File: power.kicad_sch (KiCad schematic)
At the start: 25 parts

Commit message: Assign 0603 footprints to all resistors
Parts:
- C66: footprint (none) -> Capacitor_SMD:C_0603_1608Metric_Pad1.08x0.95mm_HandSolder
- R10, R11, R8, R9: footprint (none) -> Resistor_SMD:R_0603_1608Metric_Pad0.98x0.95mm_HandSolder
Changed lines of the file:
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@@
 			)
 		)
-		(property "Footprint" ""
+		(property "Footprint" "Resistor_SMD:R_0603_1608Metric_Pad0.98x0.95mm_HandSolder"
 			(at 83.058 81.28 90)
 			(effects
@@
 			)
 		)
-		(property "Footprint" ""
+		(property "Footprint" "Resistor_SMD:R_0603_1608Metric_Pad0.98x0.95mm_HandSolder"
 			(at 111.252 69.85 90)
 			(effects
@@
 			)
 		)
-		(property "Footprint" ""
+		(property "Footprint" "Resistor_SMD:R_0603_1608Metric_Pad0.98x0.95mm_HandSolder"
 			(at 83.058 66.04 90)
 			(effects
@@
 			)
 		)
-		(property "Footprint" ""
+		(property "Footprint" "Capacitor_SMD:C_0603_1608Metric_Pad1.08x0.95mm_HandSolder"
 			(at 133.0452 132.08 0)
 			(effects
@@
 			)
 		)
-		(property "Footprint" ""
+		(property "Footprint" "Resistor_SMD:R_0603_1608Metric_Pad0.98x0.95mm_HandSolder"
 			(at 203.962 132.08 90)
 			(effects

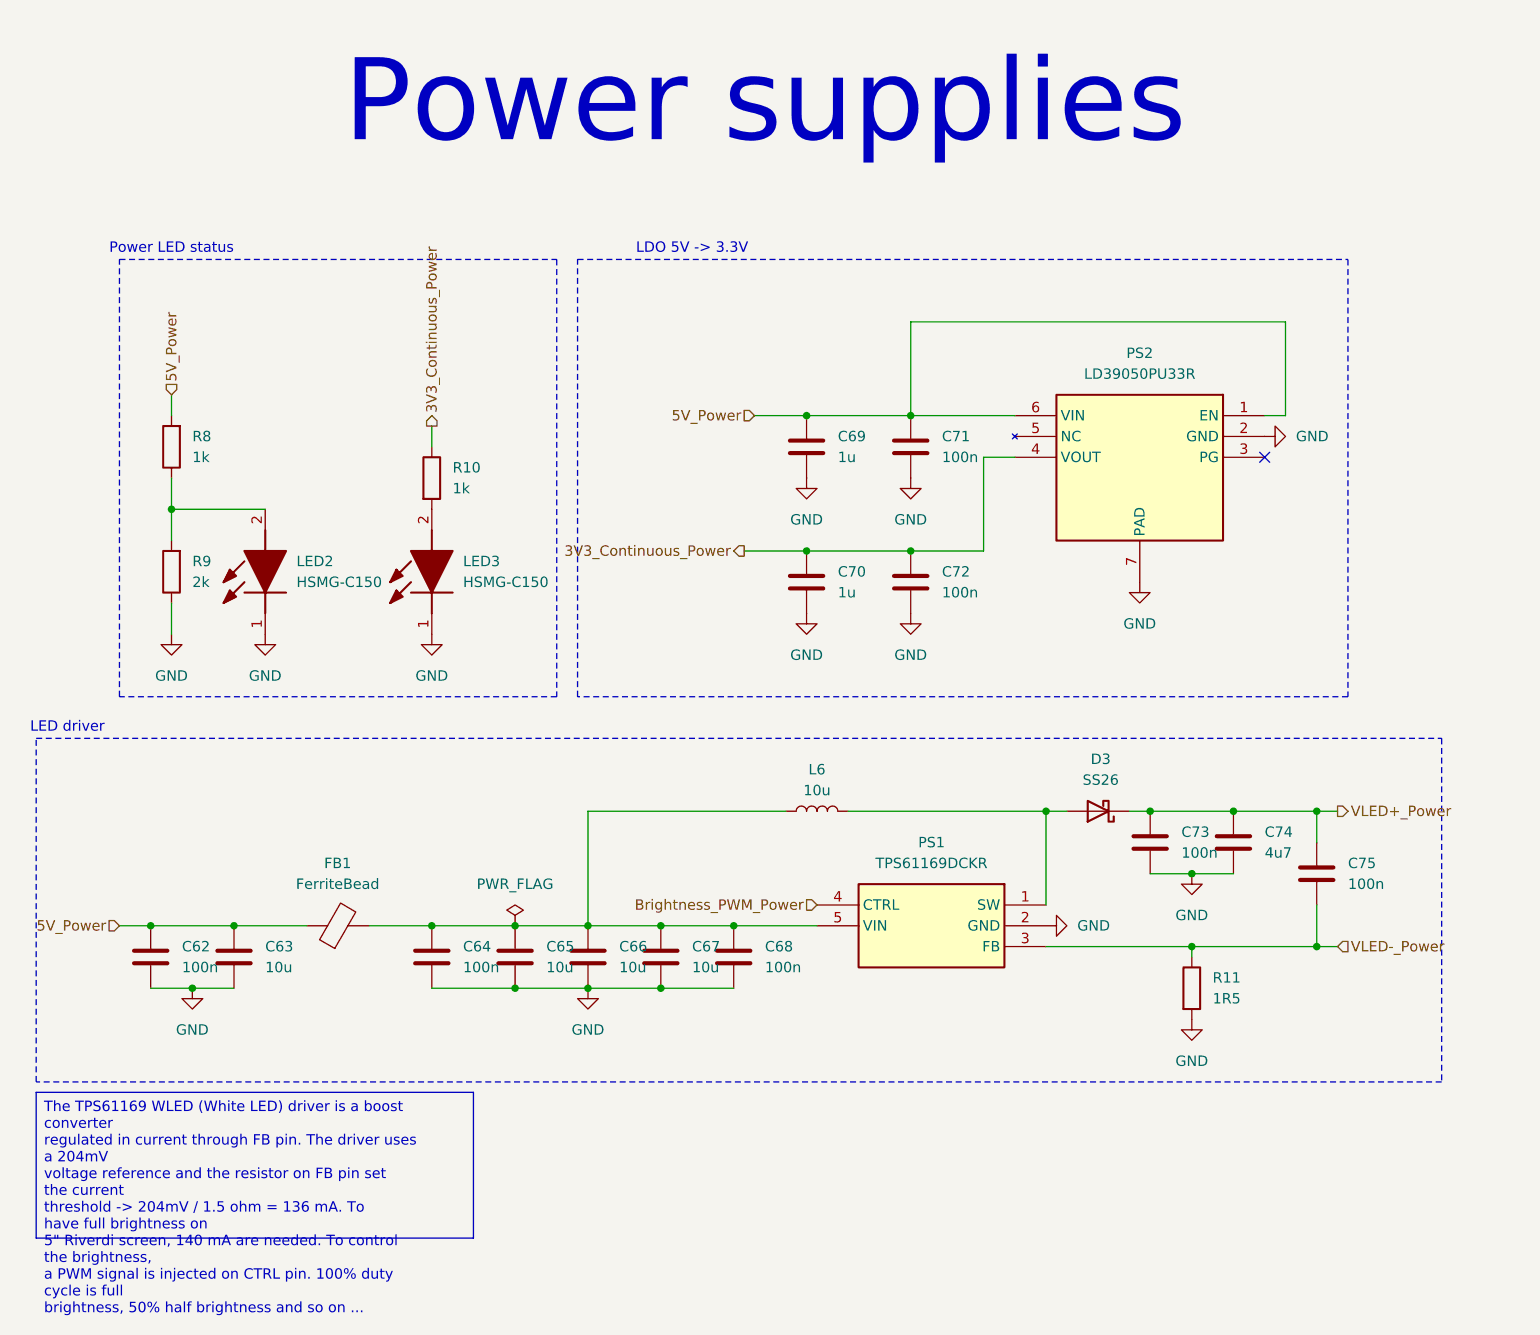
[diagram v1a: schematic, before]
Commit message: Add SS26FL diode for LCD power supply
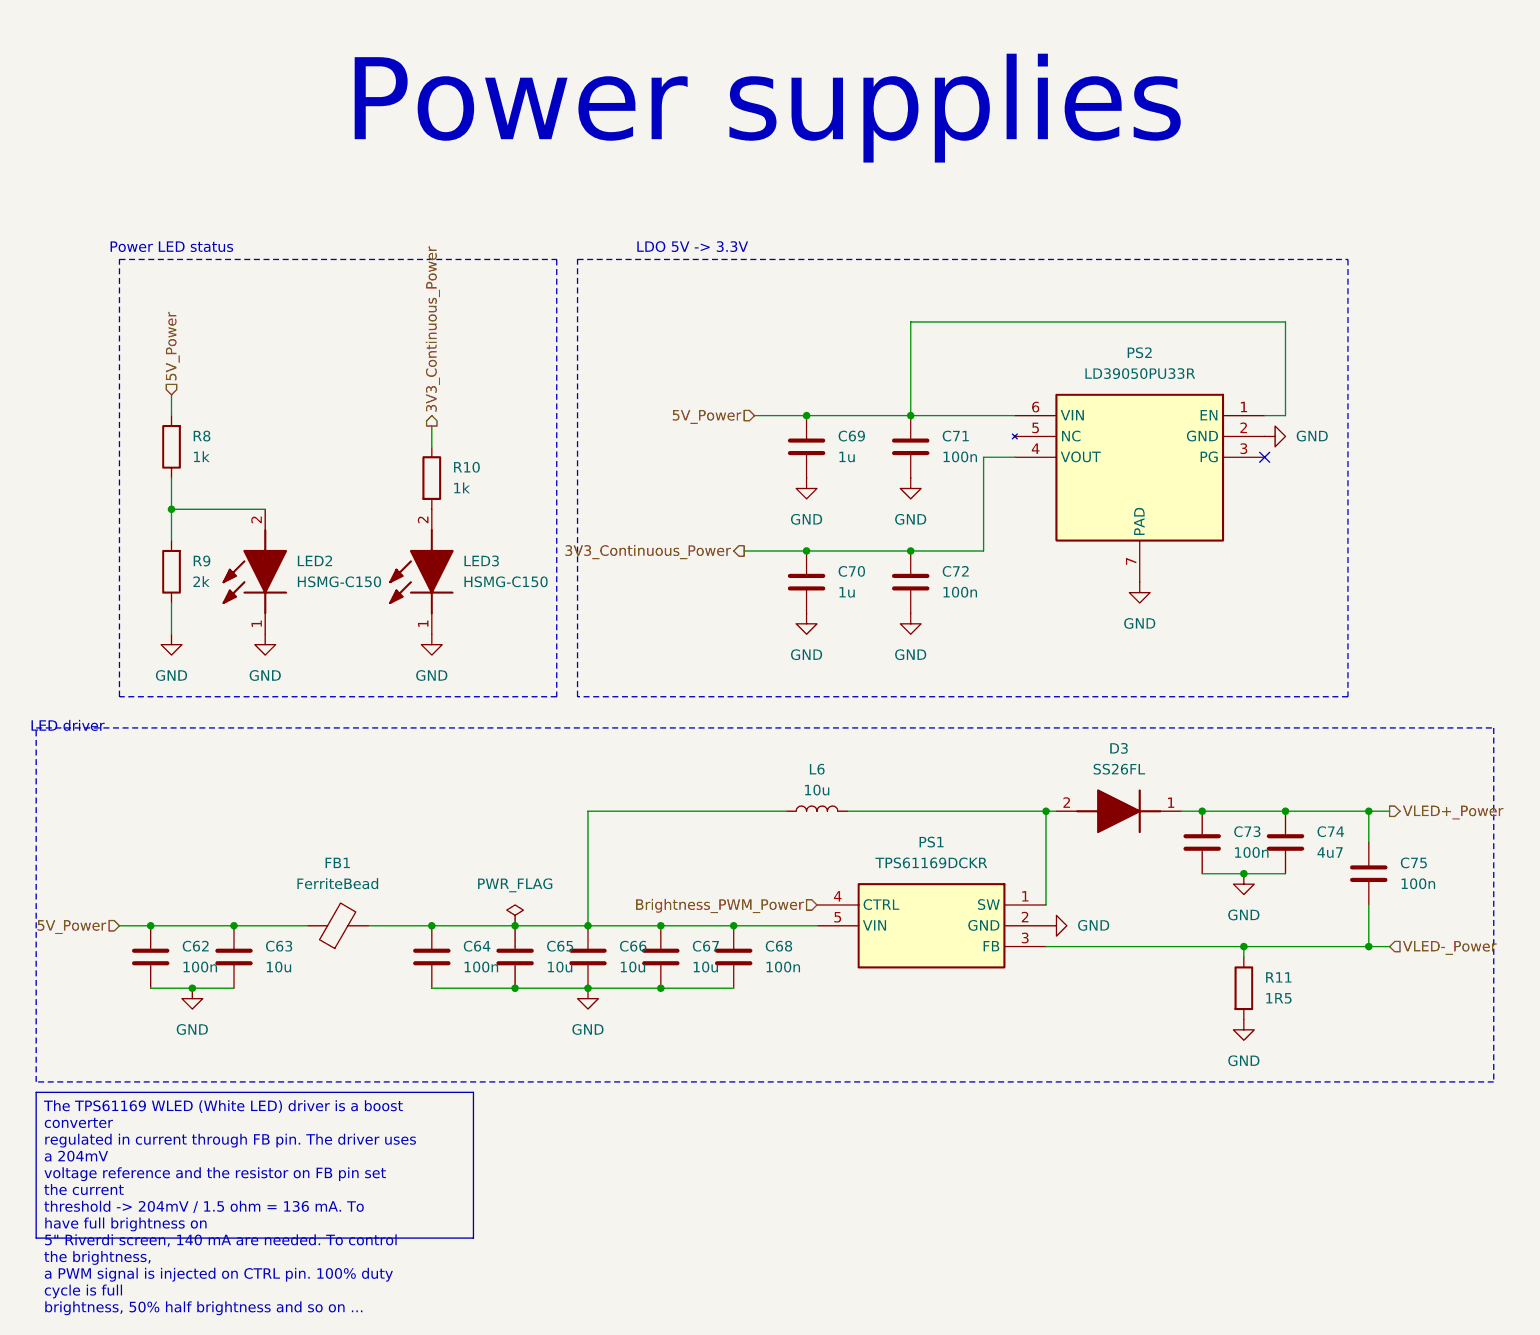
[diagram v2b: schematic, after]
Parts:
- removed D3: SS26, Diode_SMD:D_SMA, symbol Diode:SS26
- added D3: SS26FL, weather-station-poc-fp:SODFL3617X108N, symbol weather-station-poc-sym:SS26FL
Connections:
- net VLED+_Power: now also D3.1 (K)
- net at L6.2, PS1.1 (SW): now also D3.2 (A)
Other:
- moved on the sheet: C73, C74, C75, R11

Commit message: Homogenation of symbols
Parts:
- removed LED3: HSMG-C150, weather-station-poc-fp:LEDC3216X120N, symbol weather-station-poc-sym:HSMG-C150
- added LED3: HSMG-C150, weather-station-poc-fp:LEDC3216X120N, symbol Device:LED
- D3: symbol weather-station-poc-sym:SS26FL -> Device:D
- LED2: symbol weather-station-poc-sym:HSMG-C150 -> Device:LED
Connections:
- net GND: now also LED3.1 (K)
- net at R10.2: now also LED3.2 (A)

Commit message: Fill the cartridge for all schematics
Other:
- company: (none) -> Julien Cruvieux
- title: (none) -> Power supplies
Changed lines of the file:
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@@
 	(generator_version "9.0")
 	(paper "A4")
+	(title_block
+		(title "Power supplies")
+		(date "2025-12-26")
+		(rev "A")
+		(company "Julien Cruvieux")
+	)
 	(rectangle
 		(start 130.81 43.18)

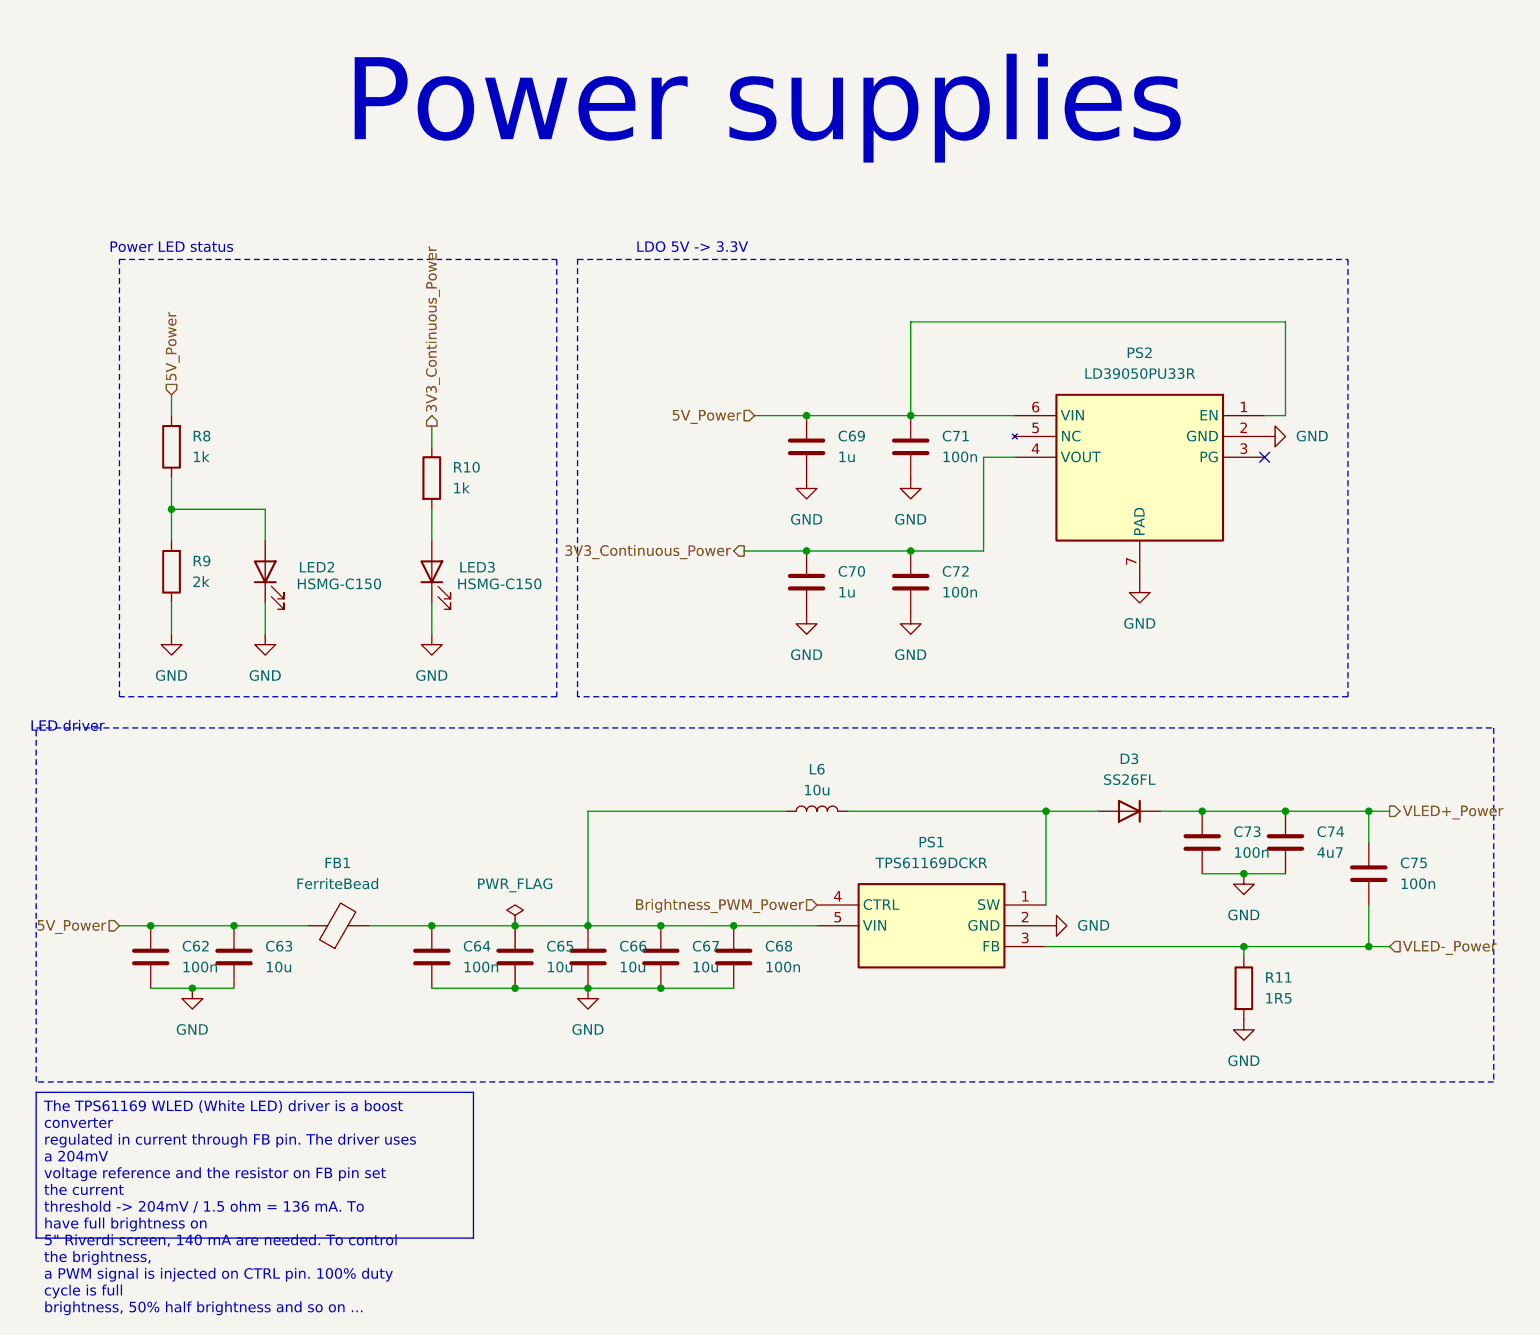
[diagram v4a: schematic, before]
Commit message: Components reindexing and update of PCB
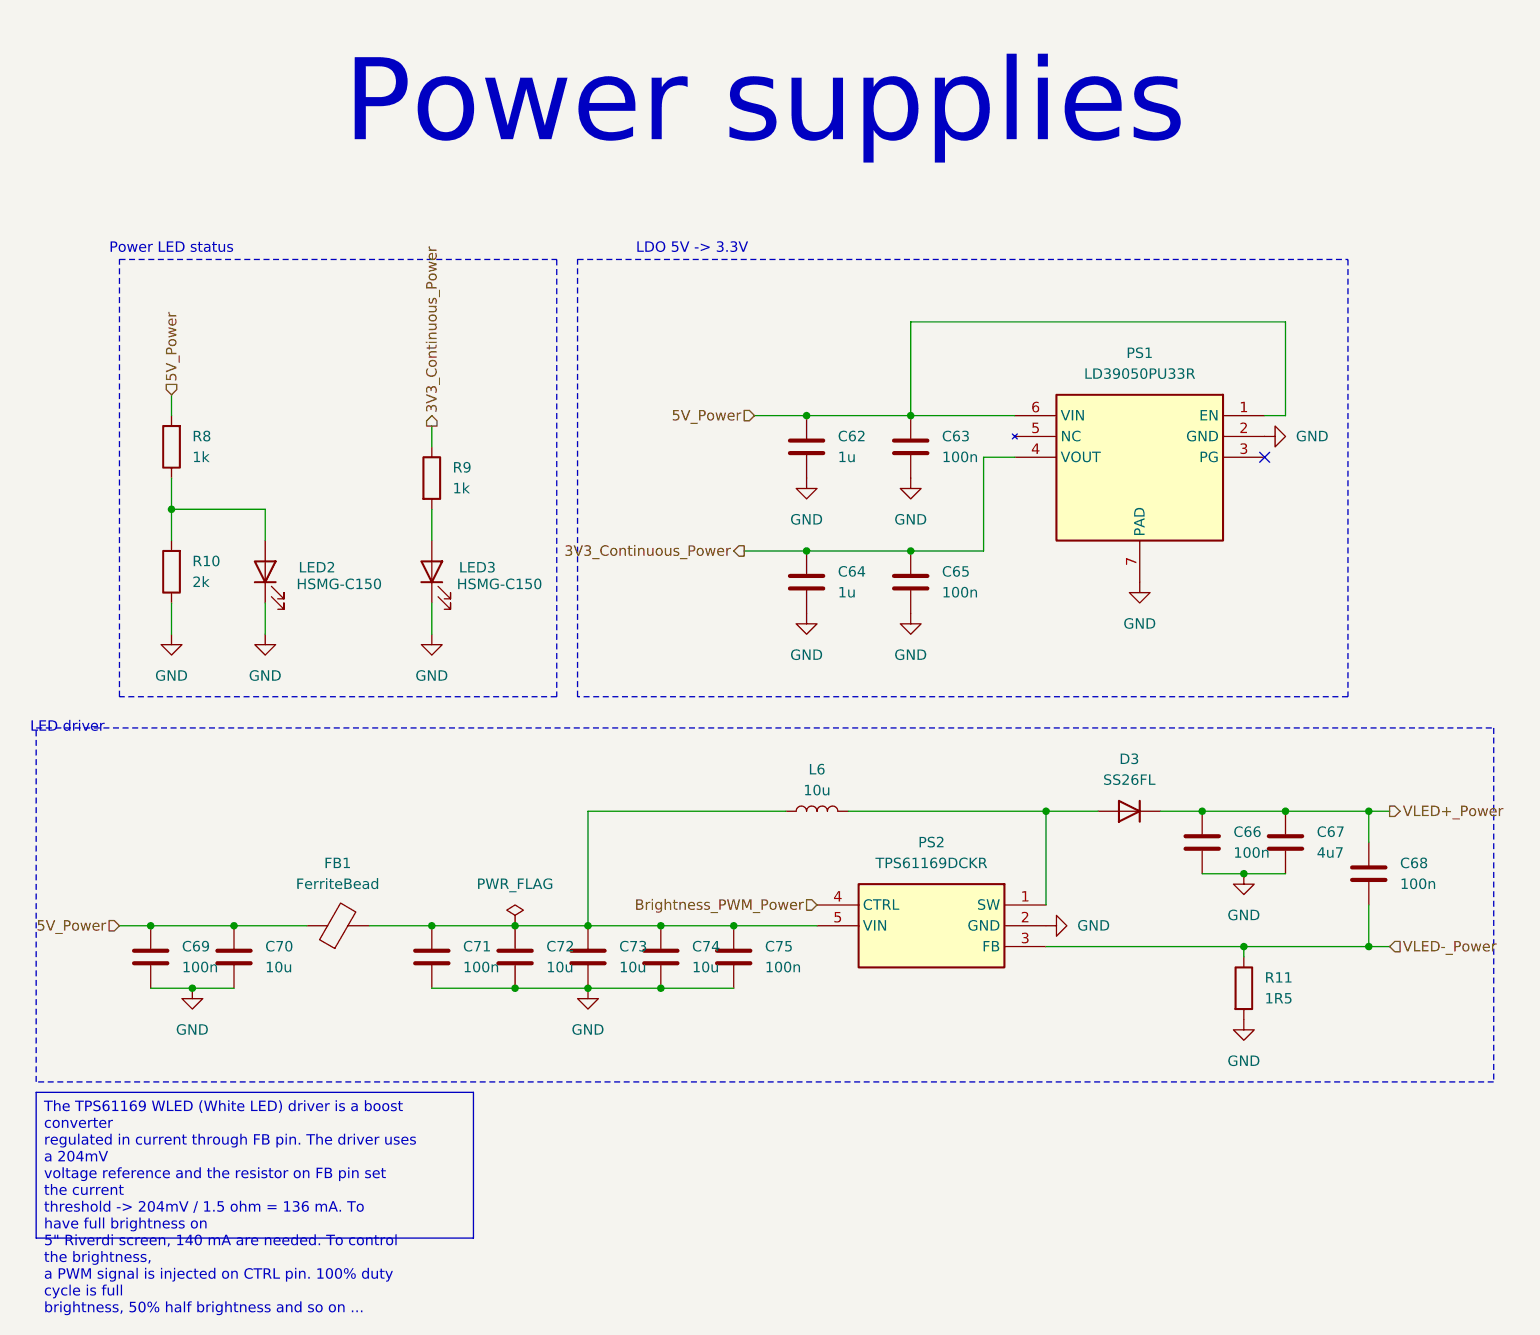
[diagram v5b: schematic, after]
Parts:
- renumbered C69 to C62, C71 to C63, C70 to C64, C72 to C65, C73 to C66, C74 to C67, C75 to C68, C62 to C69, C63 to C70, C64 to C71, C65 to C72, C66 to C73, C67 to C74, C68 to C75, PS2 to PS1, PS1 to PS2, R9 to R10, R10 to R9

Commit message: Add a new reference for L6 inductor on boost converter
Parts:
- L6: footprint (none) -> weather-station-poc-fp:INDPM4040X180N
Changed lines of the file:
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@@
 			)
 		)
-		(property "Footprint" ""
+		(property "Footprint" "weather-station-poc-fp:INDPM4040X180N"
 			(at 160.02 110.49 0)
 			(effects
@@
 			)
 		)
-		(property "Datasheet" "~"
+		(property "Datasheet" "https://www.we-online.com/components/products/datasheet/74404042100.pdf"
 			(at 160.02 110.49 0)
 			(effects
